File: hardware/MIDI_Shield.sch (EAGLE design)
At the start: 24 parts, among them U1 ARDUINO_SHIELDLABEL

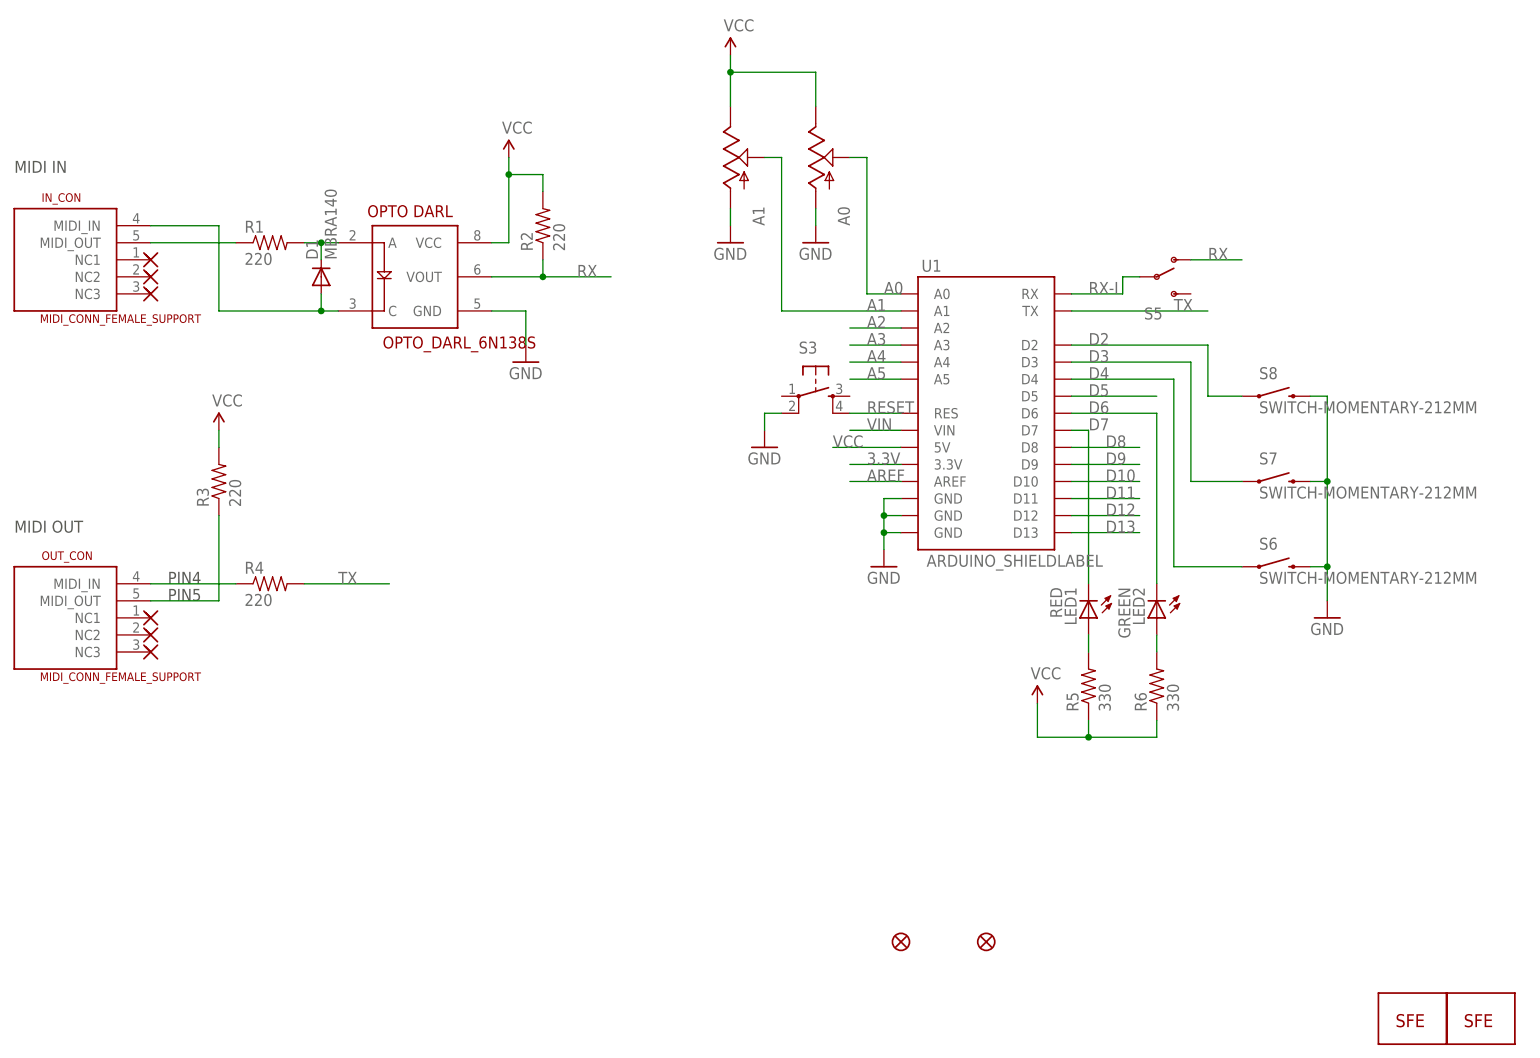
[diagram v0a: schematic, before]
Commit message: Added pin 2 ground, 0603, oshw, v#, trace/sch rework
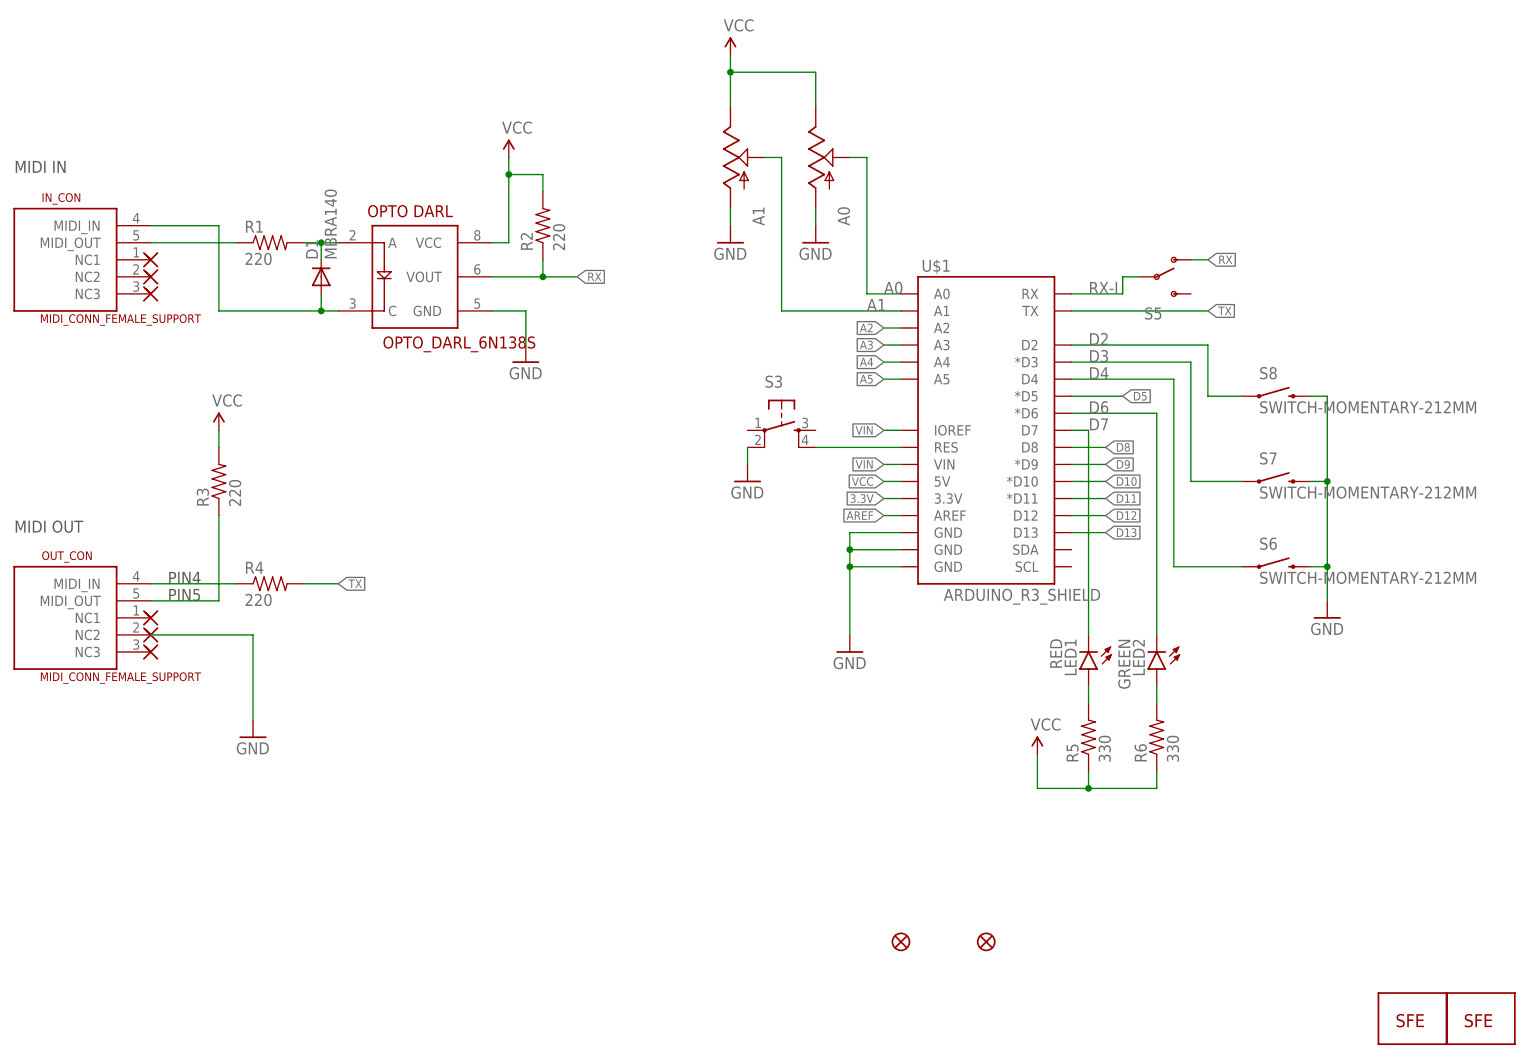
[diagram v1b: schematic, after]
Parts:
- removed U1: ARDUINO_SHIELDLABEL, SparkFun:ARDUINO_SHIELDLABEL
- added U$1: ARDUINO_R3_SHIELD, SparkFun-Boards:ARDUINO_R3_SHIELD
- LED1: device SparkFun:LED0603 -> SparkFun-LED:LED-RED0603
- LED2: device SparkFun:LED0603 -> SparkFun-LED:LED-GREEN0603
- R1, R2, R3, R4: device SparkFun:RESISTOR0402-RES -> SparkFun-Resistors:220KOHM1/10W1%(0603)
- R5, R6: device SparkFun:RESISTOR0402-RES -> SparkFun-Resistors:330OHM1/10W1%(0603)
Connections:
- removed net RESET: S3.4, U1.RES
- net 3.3V: now also U$1.3.3V; no longer U1.3.3V
- net A0: now also U$1.A0; no longer U1.A0
- net A1: now also U$1.A1; no longer U1.A1
- net A2: now also U$1.A2; no longer U1.A2
- net A3: now also U$1.A3; no longer U1.A3
- net A4: now also U$1.A4; no longer U1.A4
- net A5: now also U$1.A5; no longer U1.A5
- net AREF: now also U$1.AREF; no longer U1.AREF
- net D10: now also U$1.*D10; no longer U1.D10
- net D11: now also U$1.*D11; no longer U1.D11
- net D12: now also U$1.D12; no longer U1.D12
- net D13: now also U$1.D13; no longer U1.D13
- net D2: now also U$1.D2; no longer U1.D2
- net D3: now also U$1.*D3; no longer U1.D3
- net D4: now also U$1.D4; no longer U1.D4
- net D5: now also U$1.*D5; no longer U1.D5
- net D6: now also U$1.*D6; no longer U1.D6
- net D7: now also U$1.D7; no longer U1.D7
- net D8: now also U$1.D8; no longer U1.D8
- net D9: now also U$1.*D9; no longer U1.D9
- net GND: now also OUT_CON.NC2, U$1.GND@0, U$1.GND@1, U$1.GND@2; no longer U1.GND@0, U1.GND@1, U1.GND@2
- net RX-I: now also U$1.RX; no longer U1.RX
- net TX: now also U$1.TX; no longer U1.TX
- net VCC: now also S3.4, U$1.5V, U$1.RES; no longer U1.5V
- net VIN: now also U$1.IOREF, U$1.VIN; no longer U1.VIN
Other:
- moved on the sheet: R5, R6, S3
